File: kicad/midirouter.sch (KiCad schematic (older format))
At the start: 27 parts, among them J2 Conn_01x08, J3 Conn_01x08, J4 Conn_01x08, J5 Conn_01x08, J6 Conn_01x08, J7 Conn_01x08, J8 Conn_01x08, J9 Conn_01x08, Q1 PN2222A, Q2 PN2222A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

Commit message: Work on schematics and pcbs.
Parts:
- U5, U6: footprint Package_SO:SOP-16_7.5x10.4mm_P1.27mm -> Package_SO:SOP-16_4.4x10.4mm_P1.27mm
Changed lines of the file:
@@
 $Descr A4 11693 8268
 encoding utf-8
-Sheet 1 3
+Sheet 1 2
 Title "MidiRouter"
 Date ""
@@
 F 0 "U5" H 7800 2766 50  0000 C CNN
 F 1 "74LS594" H 7800 2675 50  0000 C CNN
-F 2 "Package_SO:SOP-16_7.5x10.4mm_P1.27mm" H 7800 1950 50  0001 C CNN
+F 2 "Package_SO:SOP-16_4.4x10.4mm_P1.27mm" H 7800 1950 50  0001 C CNN
 F 3 "" H 7800 1950 50  0001 C CNN
 	1    7800 1950
@@
 F 0 "U6" H 7800 4766 50  0000 C CNN
 F 1 "74LS594" H 7800 4675 50  0000 C CNN
-F 2 "Package_SO:SOP-16_7.5x10.4mm_P1.27mm" H 7800 3950 50  0001 C CNN
+F 2 "Package_SO:SOP-16_4.4x10.4mm_P1.27mm" H 7800 3950 50  0001 C CNN
 F 3 "" H 7800 3950 50  0001 C CNN
 	1    7800 3950

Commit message: Work on pcbs a bit.
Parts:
- removed U5, U6: 74LS594, Package_SO:SOP-16_4.4x10.4mm_P1.27mm, symbol 74xx_IEEE:74LS594
- added U5, U6: 74LS595, Package_SO:SOP-16_4.4x10.4mm_P1.27mm, symbol 74xx_IEEE:74LS595
- Q1, Q2, Q3, Q4: footprint Package_TO_SOT_THT:TO-92_Inline -> Tomarus:MMBT2222A-SOT23
- R17, R18, R19, R20, R21, R22, R23, R24, R25, R26, R27, R28: footprint Resistor_SMD:R_1206_3216Metric_Pad1.42x1.75mm_HandSolder -> Resistor_SMD:R_0805_2012Metric_Pad1.15x1.40mm_HandSolder
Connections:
- net +3V3: now also U5.10 (~SCLR), U6.10 (~SCLR)
- net GND: now also U5.13 (~G), U5.8 (GND), U6.13 (~G), U6.8 (GND)
- net VCC: now also U5.16 (VCC), U6.16 (VCC)
- net at R18.2: now also U5.1 (QB)
- net at U7.31 (U1): now also U5.11 (SCLK), U6.11 (SCLK)
- net at U7.30 (T2): now also U5.12 (RCLK), U6.12 (RCLK)
- net at U7.32 (W2): now also U5.14 (SER)
- net at R17.2: now also U5.15 (QA)
- net at R19.2: now also U5.2 (QC)
- net at R20.2: now also U5.3 (QD)
- net at R21.2: now also U5.4 (QE)
- net at R22.2: now also U5.5 (QF)
- net at R23.2: now also U5.6 (QG)
- net at R24.2: now also U5.7 (QH)
- net at R25.2: now also U6.1 (QB)
- net at R26.2: now also U6.2 (QC)
- net at R27.2: now also U6.3 (QD)
- net at R28.2: now also U6.4 (QE)
- new net: U5.9 (QHser), U6.14 (SER)
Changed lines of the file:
@@
 $EndDescr
-$Comp
-L 74xx_IEEE:74LS594 U5
-U 1 1 5C1969E5
-P 7800 1950
-F 0 "U5" H 7800 2766 50  0000 C CNN
-F 1 "74LS594" H 7800 2675 50  0000 C CNN
-F 2 "Package_SO:SOP-16_4.4x10.4mm_P1.27mm" H 7800 1950 50  0001 C CNN
-F 3 "" H 7800 1950 50  0001 C CNN
-	1    7800 1950
-	1    0    0    -1
-$EndComp
-$Comp
-L 74xx_IEEE:74LS594 U6
-U 1 1 5C196B92
-P 7800 3950
-F 0 "U6" H 7800 4766 50  0000 C CNN
-F 1 "74LS594" H 7800 4675 50  0000 C CNN
-F 2 "Package_SO:SOP-16_4.4x10.4mm_P1.27mm" H 7800 3950 50  0001 C CNN
-F 3 "" H 7800 3950 50  0001 C CNN
-	1    7800 3950
-	1    0    0    -1
-$EndComp
 $Comp
 L Transistor_BJT:PN2222A Q4
@@
 F 0 "Q4" V 10536 4250 50  0000 C CNN
 F 1 "PN2222A" V 10627 4250 50  0000 C CNN
-F 2 "Package_TO_SOT_THT:TO-92_Inline" H 10500 4175 50  0001 L CIN
+F 2 "Tomarus:MMBT2222A-SOT23" H 10500 4175 50  0001 L CIN
 F 3 "http://www.fairchildsemi.com/ds/PN/PN2222A.pdf" H 10300 4250 50  0001 L CNN
 	1    10300 4250
@@
 F 0 "Q3" V 10036 4350 50  0000 C CNN
 F 1 "PN2222A" V 10127 4350 50  0000 C CNN
-F 2 "Package_TO_SOT_THT:TO-92_Inline" H 10000 4275 50  0001 L CIN
+F 2 "Tomarus:MMBT2222A-SOT23" H 10000 4275 50  0001 L CIN
 F 3 "http://www.fairchildsemi.com/ds/PN/PN2222A.pdf" H 9800 4350 50  0001 L CNN
 	1    9800 4350
@@
 F 0 "Q2" V 9536 4450 50  0000 C CNN
 F 1 "PN2222A" V 9627 4450 50  0000 C CNN
-F 2 "Package_TO_SOT_THT:TO-92_Inline" H 9500 4375 50  0001 L CIN
+F 2 "Tomarus:MMBT2222A-SOT23" H 9500 4375 50  0001 L CIN
 F 3 "http://www.fairchildsemi.com/ds/PN/PN2222A.pdf" H 9300 4450 50  0001 L CNN
 	1    9300 4450
@@
 F 0 "Q1" V 9036 4550 50  0000 C CNN
 F 1 "PN2222A" V 9127 4550 50  0000 C CNN
-F 2 "Package_TO_SOT_THT:TO-92_Inline" H 9000 4475 50  0001 L CIN
+F 2 "Tomarus:MMBT2222A-SOT23" H 9000 4475 50  0001 L CIN
 F 3 "http://www.fairchildsemi.com/ds/PN/PN2222A.pdf" H 8800 4550 50  0001 L CNN
 	1    8800 4550
@@
 F 0 "R17" V 8450 2150 50  0000 C CNN
 F 1 "220" V 8500 1950 50  0000 C CNN
-F 2 "Resistor_SMD:R_1206_3216Metric_Pad1.42x1.75mm_HandSolder" V 8430 1950 50  0001 C CNN
+F 2 "Resistor_SMD:R_0805_2012Metric_Pad1.15x1.40mm_HandSolder" V 8430 1950 50  0001 C CNN
 F 3 "~" H 8500 1950 50  0001 C CNN
 	1    8500 1950
@@
 F 0 "R18" V 8450 2250 50  0000 C CNN
 F 1 "220" V 8500 2050 50  0000 C CNN
-F 2 "Resistor_SMD:R_1206_3216Metric_Pad1.42x1.75mm_HandSolder" V 8430 2050 50  0001 C CNN
+F 2 "Resistor_SMD:R_0805_2012Metric_Pad1.15x1.40mm_HandSolder" V 8430 2050 50  0001 C CNN
 F 3 "~" H 8500 2050 50  0001 C CNN
 	1    8500 2050
@@
 F 0 "R19" V 8450 2350 50  0000 C CNN
 F 1 "220" V 8500 2150 50  0000 C CNN
-F 2 "Resistor_SMD:R_1206_3216Metric_Pad1.42x1.75mm_HandSolder" V 8430 2150 50  0001 C CNN
+F 2 "Resistor_SMD:R_0805_2012Metric_Pad1.15x1.40mm_HandSolder" V 8430 2150 50  0001 C CNN
 F 3 "~" H 8500 2150 50  0001 C CNN
 	1    8500 2150
@@
 F 0 "R20" V 8450 2450 50  0000 C CNN
 F 1 "220" V 8500 2250 50  0000 C CNN
-F 2 "Resistor_SMD:R_1206_3216Metric_Pad1.42x1.75mm_HandSolder" V 8430 2250 50  0001 C CNN
+F 2 "Resistor_SMD:R_0805_2012Metric_Pad1.15x1.40mm_HandSolder" V 8430 2250 50  0001 C CNN
 F 3 "~" H 8500 2250 50  0001 C CNN
 	1    8500 2250
@@
 F 0 "R21" V 8450 2550 50  0000 C CNN
 F 1 "220" V 8500 2350 50  0000 C CNN
-F 2 "Resistor_SMD:R_1206_3216Metric_Pad1.42x1.75mm_HandSolder" V 8430 2350 50  0001 C CNN
+F 2 "Resistor_SMD:R_0805_2012Metric_Pad1.15x1.40mm_HandSolder" V 8430 2350 50  0001 C CNN
 F 3 "~" H 8500 2350 50  0001 C CNN
 	1    8500 2350
@@
 F 0 "R22" V 8450 2650 50  0000 C CNN
 F 1 "220" V 8500 2450 50  0000 C CNN
-F 2 "Resistor_SMD:R_1206_3216Metric_Pad1.42x1.75mm_HandSolder" V 8430 2450 50  0001 C CNN
+F 2 "Resistor_SMD:R_0805_2012Metric_Pad1.15x1.40mm_HandSolder" V 8430 2450 50  0001 C CNN
 F 3 "~" H 8500 2450 50  0001 C CNN
 	1    8500 2450
@@
 F 0 "R23" V 8450 2750 50  0000 C CNN
 F 1 "220" V 8500 2550 50  0000 C CNN
-F 2 "Resistor_SMD:R_1206_3216Metric_Pad1.42x1.75mm_HandSolder" V 8430 2550 50  0001 C CNN
+F 2 "Resistor_SMD:R_0805_2012Metric_Pad1.15x1.40mm_HandSolder" V 8430 2550 50  0001 C CNN
 F 3 "~" H 8500 2550 50  0001 C CNN
 	1    8500 2550
@@
 F 0 "R24" V 8450 2850 50  0000 C CNN
 F 1 "220" V 8500 2650 50  0000 C CNN
-F 2 "Resistor_SMD:R_1206_3216Metric_Pad1.42x1.75mm_HandSolder" V 8430 2650 50  0001 C CNN
+F 2 "Resistor_SMD:R_0805_2012Metric_Pad1.15x1.40mm_HandSolder" V 8430 2650 50  0001 C CNN
 F 3 "~" H 8500 2650 50  0001 C CNN
 	1    8500 2650
@@
 F 0 "R25" V 8450 4250 50  0000 C CNN
 F 1 "3300" V 8500 4050 50  0000 C CNN
-F 2 "Resistor_SMD:R_1206_3216Metric_Pad1.42x1.75mm_HandSolder" V 8430 4050 50  0001 C CNN
+F 2 "Resistor_SMD:R_0805_2012Metric_Pad1.15x1.40mm_HandSolder" V 8430 4050 50  0001 C CNN
 F 3 "~" H 8500 4050 50  0001 C CNN
 	1    8500 4050
@@
 F 0 "R26" V 8450 4350 50  0000 C CNN
 F 1 "3300" V 8500 4150 50  0000 C CNN
-F 2 "Resistor_SMD:R_1206_3216Metric_Pad1.42x1.75mm_HandSolder" V 8430 4150 50  0001 C CNN
+F 2 "Resistor_SMD:R_0805_2012Metric_Pad1.15x1.40mm_HandSolder" V 8430 4150 50  0001 C CNN
 F 3 "~" H 8500 4150 50  0001 C CNN
 	1    8500 4150
@@
 F 0 "R27" V 8450 4450 50  0000 C CNN
 F 1 "3300" V 8500 4250 50  0000 C CNN
-F 2 "Resistor_SMD:R_1206_3216Metric_Pad1.42x1.75mm_HandSolder" V 8430 4250 50  0001 C CNN
+F 2 "Resistor_SMD:R_0805_2012Metric_Pad1.15x1.40mm_HandSolder" V 8430 4250 50  0001 C CNN
 F 3 "~" H 8500 4250 50  0001 C CNN
 	1    8500 4250
@@
 F 0 "R28" V 8450 4550 50  0000 C CNN
 F 1 "3300" V 8500 4350 50  0000 C CNN
-F 2 "Resistor_SMD:R_1206_3216Metric_Pad1.42x1.75mm_HandSolder" V 8430 4350 50  0001 C CNN
+F 2 "Resistor_SMD:R_0805_2012Metric_Pad1.15x1.40mm_HandSolder" V 8430 4350 50  0001 C CNN
 F 3 "~" H 8500 4350 50  0001 C CNN
 	1    8500 4350
@@
 	10500 4350 10600 4350
 $Comp
-L power:+3.3V #PWR022
-U 1 1 5C49138F
-P 7250 3400
-F 0 "#PWR022" H 7250 3250 50  0001 C CNN
-F 1 "+3.3V" V 7265 3528 50  0000 L CNN
-F 2 "" H 7250 3400 50  0001 C CNN
-F 3 "" H 7250 3400 50  0001 C CNN
-	1    7250 3400
-	0    -1   -1   0
-$EndComp
-$Comp
 L power:+3.3V #PWR023
 U 1 1 5C4BE539
@@
 $EndComp
 $Comp
-L power:+3.3V #PWR020
-U 1 1 5C4BEB6D
-P 7250 1400
-F 0 "#PWR020" H 7250 1250 50  0001 C CNN
-F 1 "+3.3V" V 7265 1528 50  0000 L CNN
-F 2 "" H 7250 1400 50  0001 C CNN
-F 3 "" H 7250 1400 50  0001 C CNN
-	1    7250 1400
-	0    -1   -1   0
-$EndComp
-$Comp
 L power:+3.3V #PWR021
 U 1 1 5C4BED4B
@@
 	6450 2350 6450 4350
 Wire Wire Line
-	8350 2750 8350 2950
-Wire Wire Line
 	6750 2950 6750 4350
 Wire Wire Line
@@
 Wire Wire Line
 	6450 2350 7250 2350
-Wire Wire Line
-	6750 2950 8350 2950
-NoConn ~ 8350 3950
-NoConn ~ 8350 4450
-NoConn ~ 8350 4550
-NoConn ~ 8350 4650
-NoConn ~ 8350 4750
+NoConn ~ 8150 3950
+NoConn ~ 8150 4450
+NoConn ~ 8150 4550
+NoConn ~ 8150 4650
+NoConn ~ 8150 4750
 NoConn ~ 5550 4950
 NoConn ~ 5550 4850
@@
 	0    -1   -1   0
 $EndComp
+$Comp
+L 74xx_IEEE:74LS595 U5
+U 1 1 5E0E8E8D
+P 7700 1950
+F 0 "U5" H 7700 2700 50  0000 C CNN
+F 1 "74LS595" H 7700 2600 50  0000 C CNN
+F 2 "Package_SO:SOP-16_4.4x10.4mm_P1.27mm" H 7700 1950 50  0001 C CNN
+F 3 "" H 7700 1950 50  0001 C CNN
+	1    7700 1950
+	1    0    0    -1
+$EndComp
+Wire Wire Line
+	8150 2750 8150 2950
+Wire Wire Line
+	8150 2950 6750 2950
+Wire Wire Line
+	8350 2650 8150 2650
+Wire Wire Line
+	8150 2550 8350 2550
+Wire Wire Line
+	8350 2450 8150 2450
+Wire Wire Line
+	8150 2350 8350 2350
+Wire Wire Line
+	8350 2250 8150 2250
+Wire Wire Line
+	8150 2150 8350 2150
+Wire Wire Line
+	8350 2050 8150 2050
+Wire Wire Line
+	8150 1950 8350 1950
+$Comp
+L power:GND #PWR0116
+U 1 1 5E0F6682
+P 7250 1400
+F 0 "#PWR0116" H 7250 1150 50  0001 C CNN
+F 1 "GND" V 7255 1272 50  0000 R CNN
+F 2 "" H 7250 1400 50  0001 C CNN
+F 3 "" H 7250 1400 50  0001 C CNN
+	1    7250 1400
+	0    1    1    0
+$EndComp
+$Comp
+L 74xx_IEEE:74LS595 U6
+U 1 1 5E0F75A2
+P 7700 3950
+F 0 "U6" H 7700 4700 50  0000 C CNN
+F 1 "74LS595" H 7700 4600 50  0000 C CNN
+F 2 "Package_SO:SOP-16_4.4x10.4mm_P1.27mm" H 7700 3950 50  0001 C CNN
+F 3 "" H 7700 3950 50  0001 C CNN
+	1    7700 3950
+	1    0    0    -1
+$EndComp
+Wire Wire Line
+	8350 4050 8150 4050
+Wire Wire Line
+	8150 4150 8350 4150
+Wire Wire Line
+	8350 4250 8150 4250
+Wire Wire Line
+	8150 4350 8350 4350
+$Comp
+L power:GND #PWR0117
+U 1 1 5E100488
+P 7250 3400
+F 0 "#PWR0117" H 7250 3150 50  0001 C CNN
+F 1 "GND" V 7255 3272 50  0000 R CNN
+F 2 "" H 7250 3400 50  0001 C CNN
+F 3 "" H 7250 3400 50  0001 C CNN
+	1    7250 3400
+	0    1    1    0
+$EndComp
 $EndSCHEMATC

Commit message: More work on pcbs and frontpanel.
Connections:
- net +5V renamed CA7_VCC
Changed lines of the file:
@@
-	0    -1   -1   0
-$EndComp
-$Comp
-L power:+5V #PWR017
-U 1 1 5C57A074
-P 4850 5050
-F 0 "#PWR017" H 4850 4900 50  0001 C CNN
-F 1 "+5V" V 4865 5178 50  0000 L CNN
-F 2 "" H 4850 5050 50  0001 C CNN
-F 3 "" H 4850 5050 50  0001 C CNN
-	1    4850 5050
 	0    -1   -1   0
 $EndComp
@@
 	1    0    0    -1
 $EndComp
-Wire Wire Line
-	4850 5050 4950 5050
 Wire Wire Line
 	5650 5050 5550 5050
@@
 	0    1    1    0
 $EndComp
+Text GLabel 4950 5050 0    50   Input ~ 0
+CA7_VCC
 $EndSCHEMATC

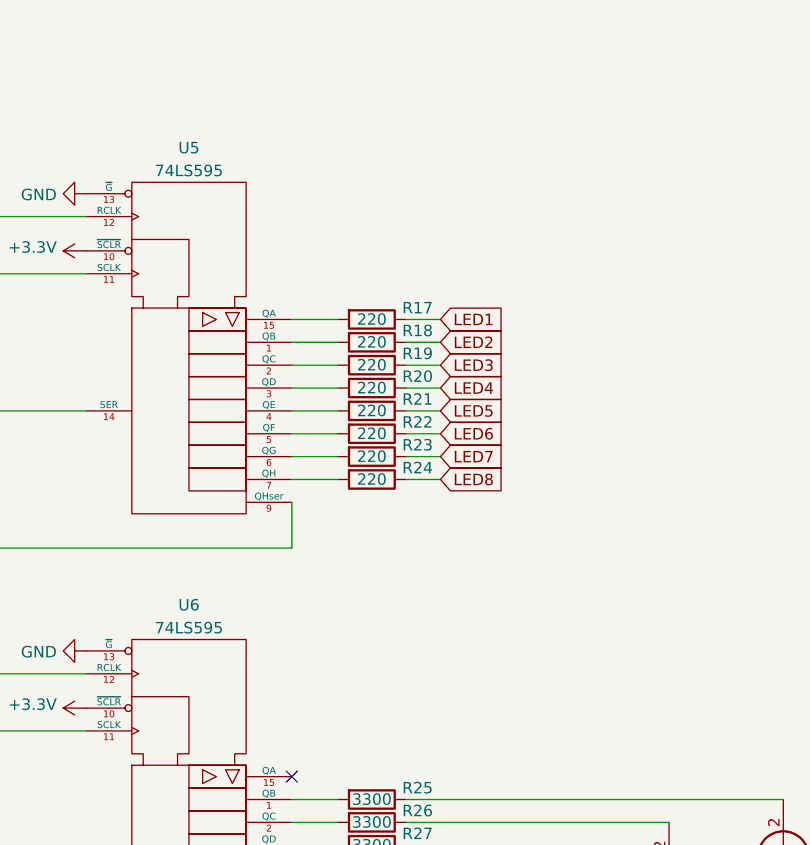
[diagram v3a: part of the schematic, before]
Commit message: Work on base pcb/schematics + frontpanel.
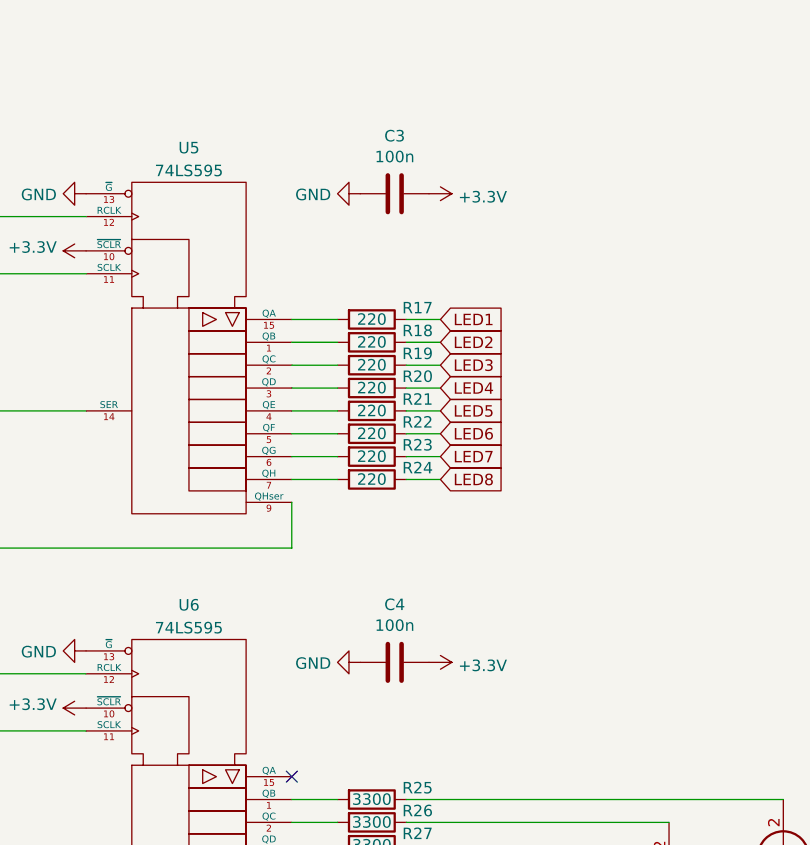
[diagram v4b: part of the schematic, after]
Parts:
- added C3, C4: 100n, Capacitor_SMD:C_0805_2012Metric, symbol Device:C
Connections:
- net +3V3: now also C3.1, C4.1
- net GND: now also C3.2, C4.2
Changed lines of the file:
@@
 Text GLabel 4950 5050 0    50   Input ~ 0
 CA7_VCC
+$Comp
+L Device:C C3
+U 1 1 5E152B2A
+P 8600 1400
+F 0 "C3" V 8348 1400 50  0000 C CNN
+F 1 "100n" V 8439 1400 50  0000 C CNN
+F 2 "Capacitor_SMD:C_0805_2012Metric" H 8638 1250 50  0001 C CNN
+F 3 "~" H 8600 1400 50  0001 C CNN
+	1    8600 1400
+	0    1    1    0
+$EndComp
+$Comp
+L power:GND #PWR03
+U 1 1 5E152BCF
+P 8450 1400
+F 0 "#PWR03" H 8450 1150 50  0001 C CNN
+F 1 "GND" V 8455 1272 50  0000 R CNN
+F 2 "" H 8450 1400 50  0001 C CNN
+F 3 "" H 8450 1400 50  0001 C CNN
+	1    8450 1400
+	0    1    1    0
+$EndComp
+$Comp
+L power:+3.3V #PWR04
+U 1 1 5E152C12
+P 8750 1400
+F 0 "#PWR04" H 8750 1250 50  0001 C CNN
+F 1 "+3.3V" V 8765 1528 50  0000 L CNN
+F 2 "" H 8750 1400 50  0001 C CNN
+F 3 "" H 8750 1400 50  0001 C CNN
+	1    8750 1400
+	0    1    1    0
+$EndComp
+$Comp
+L Device:C C4
+U 1 1 5E152D0E
+P 8600 3450
+F 0 "C4" V 8348 3450 50  0000 C CNN
+F 1 "100n" V 8439 3450 50  0000 C CNN
+F 2 "Capacitor_SMD:C_0805_2012Metric" H 8638 3300 50  0001 C CNN
+F 3 "~" H 8600 3450 50  0001 C CNN
+	1    8600 3450
+	0    1    1    0
+$EndComp
+$Comp
+L power:GND #PWR05
+U 1 1 5E152D15
+P 8450 3450
+F 0 "#PWR05" H 8450 3200 50  0001 C CNN
+F 1 "GND" V 8455 3322 50  0000 R CNN
+F 2 "" H 8450 3450 50  0001 C CNN
+F 3 "" H 8450 3450 50  0001 C CNN
+	1    8450 3450
+	0    1    1    0
+$EndComp
+$Comp
+L power:+3.3V #PWR06
+U 1 1 5E152D1B
+P 8750 3450
+F 0 "#PWR06" H 8750 3300 50  0001 C CNN
+F 1 "+3.3V" V 8765 3578 50  0000 L CNN
+F 2 "" H 8750 3450 50  0001 C CNN
+F 3 "" H 8750 3450 50  0001 C CNN
+	1    8750 3450
+	0    1    1    0
+$EndComp
 $EndSCHEMATC
